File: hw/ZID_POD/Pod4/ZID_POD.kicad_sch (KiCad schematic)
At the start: 2 parts, among them J1 FFC/FPC-40 Socket

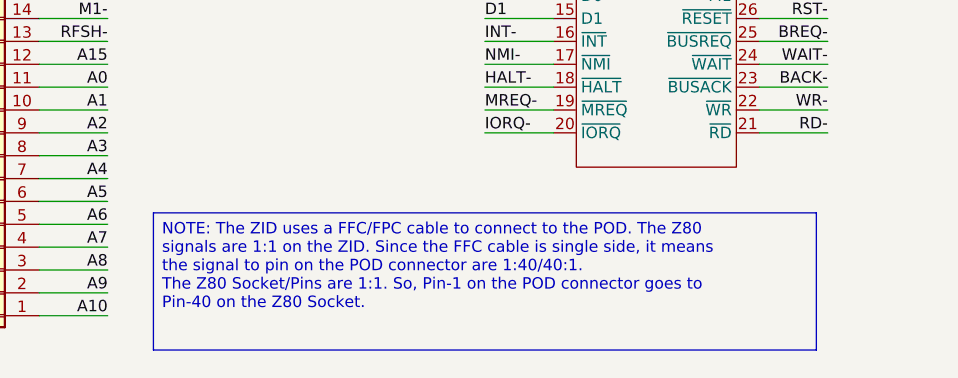
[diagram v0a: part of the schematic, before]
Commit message: PCB: Ready to order - ZID, POD1, POD2, POD3, POD4, ExpBP
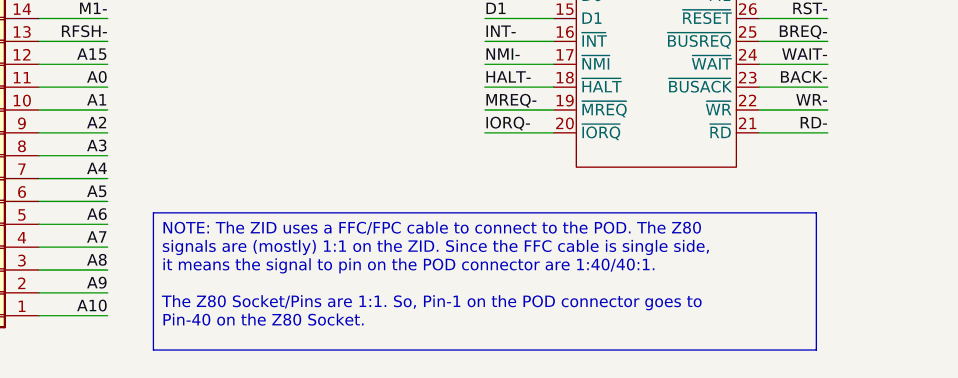
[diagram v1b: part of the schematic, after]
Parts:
- J1: footprint (none) -> AES_Library:CviLux_CF20401V_NH_FFC-FPC-AES
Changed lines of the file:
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@@
 	(title_block
 		(title "ZID POD (4)")
-		(date "2026-04-21")
+		(date "2026-08-16")
 		(rev "PR1.0")
 		(company "SilkyDESIGN")
@@
 		(comment 4 "Layout 4 of 4 to accommodate different")
 	)
-	(text_box "NOTE: The ZID uses a FFC/FPC cable to connect to the POD. The Z80 signals are 1:1 on the ZID. Since the FFC cable is single side, it means the signal to pin on the POD connector are 1:40/40:1.\nThe Z80 Socket/Pins are 1:1. So, Pin-1 on the POD connector goes to Pin-40 on the Z80 Socket."
+	(text_box "NOTE: The ZID uses a FFC/FPC cable to connect to the POD. The Z80 signals are (mostly) 1:1 on the ZID. Since the FFC cable is single side, it means the signal to pin on the POD connector are 1:40/40:1.\n\nThe Z80 Socket/Pins are 1:1. So, Pin-1 on the POD connector goes to Pin-40 on the Z80 Socket."
 		(exclude_from_sim no)
 		(at 121.92 139.7 0)
@@
 		)
 		(instances
-			(project ""
+			(project "ZID_POD"
 				(path "/5064845c-49f8-454d-ae5f-d06818afd8fe"
 					(reference "Z80-SKT1")
@@
 			)
 		)
-		(property "Footprint" ""
+		(property "Footprint" "AES_Library:CviLux_CF20401V_NH_FFC-FPC-AES"
 			(at 104.14 102.87 0)
 			(effects
